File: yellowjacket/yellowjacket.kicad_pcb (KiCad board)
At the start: 2 copper layers, 115 x 84.2 mm, 22 parts, among them SW1 SW_PUSH, SW10 SW_PUSH, SW11 SW_PUSH, SW12 SW_PUSH, SW13 SW_PUSH, SW14 SW_PUSH, SW15 SW_PUSH, SW16 SW_PUSH, SW2 SW_PUSH, SW3 SW_PUSH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

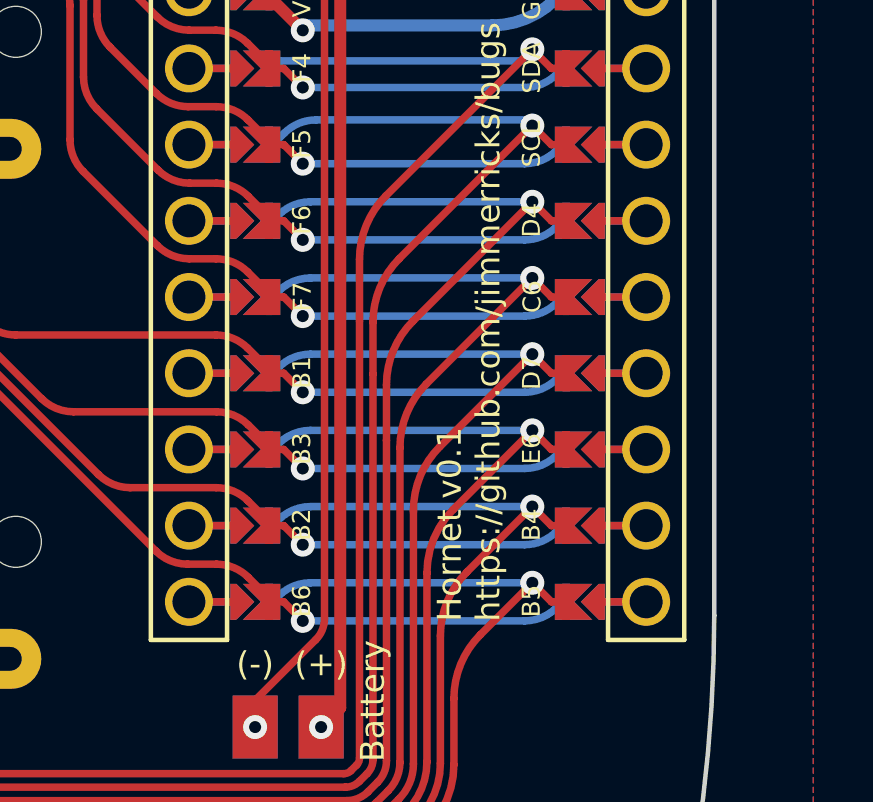
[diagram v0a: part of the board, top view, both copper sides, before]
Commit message: Renamed Hornet to Yellowjacket.
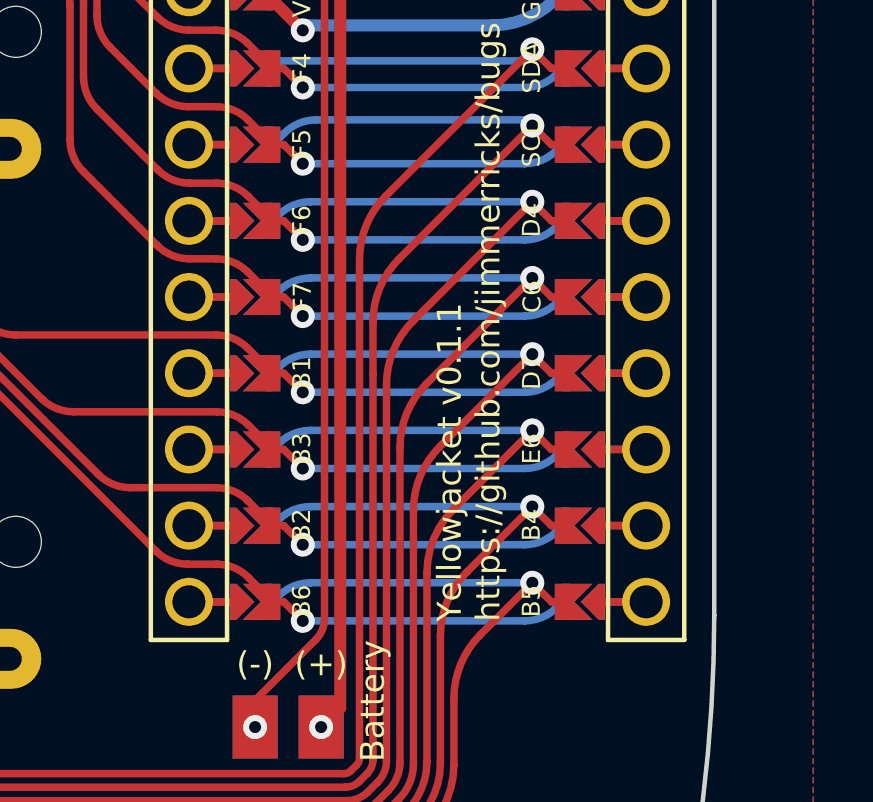
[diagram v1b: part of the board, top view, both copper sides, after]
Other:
- board text added: "Yellowjacket v0.1.1 https://github.com/jimmerricks/bugs"
- board text removed: "Hornet v0.1 https://github.com/jimmerricks/bugs"
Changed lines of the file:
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@@
   (paper "A4")
   (title_block
-    (title "Hornet")
-    (date "2021-10-11")
-    (rev "0.1")
+    (title "Yellowjacket")
+    (date "2021-10-28")
+    (rev "0.1.1")
     (company "jmnw")
   )
@@
   (gr_line (start 139.336399 45.280745) (end 139.310739 54.770533) (layer "Edge.Cuts") (width 0.15))
   (gr_arc (start 141.310739 54.770531) (end 139.310739 54.770533) (angle -90) (layer "Edge.Cuts") (width 0.15))
-  (gr_text "Hornet v0.1\nhttps://github.com/jimmerricks/bugs" (at 149.94 66.220003 90) (layer "B.SilkS")
+  (gr_text "Yellowjacket v0.1.1\nhttps://github.com/jimmerricks/bugs" (at 149.94 66.220003 90) (layer "B.SilkS")
     (effects (font (size 0.8 0.8) (thickness 0.1)) (justify left mirror))
   )
-  (gr_text "Hornet v0.1\nhttps://github.com/jimmerricks/bugs" (at 149.94 89.44 90) (layer "F.SilkS")
+  (gr_text "Yellowjacket v0.1.1\nhttps://github.com/jimmerricks/bugs" (at 149.94 89.44 90) (layer "F.SilkS")
     (effects (font (size 0.8 0.8) (thickness 0.1)) (justify left))
   )
